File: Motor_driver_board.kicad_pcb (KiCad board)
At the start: 2 copper layers, 20 parts, among them J1 USB_B_Micro, U1 LM2596DSADJG, U10 NTMFS5C628NLT1G, U11 NTMFS5C628NLT1G, U12 NTMFS5C628NLT1G, U13 LM393, U2 TPS62A01ADRL, U3 ESP32-S3-MINI-1, U4 USBLC6-2SC6, U5 DRV8323RSRGZR, U6 NTMFS5C628NLT1G, U7 NTMFS5C628NLT1G, U8 NTMFS5C628NLT1G, U9 NTMFS5C628NLT1G

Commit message: Layed out PCB
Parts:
- added C1: 470 uF, Capacitor_SMD:CP_Elec_10x12.5, F.Cu at (171.5, 55.1)
- added C10: 22 uF, Capacitor_SMD:C_0603_1608Metric, F.Cu at (174.1, 130.7)
- added C11: 1 uF, Capacitor_SMD:C_0402_1005Metric, F.Cu at (149.4, 125.2)
- added C12: 0.1 uF, Capacitor_SMD:C_0402_1005Metric, F.Cu at (178.4, 91.9)
- added C13: 1 uF, Capacitor_SMD:C_0402_1005Metric, F.Cu at (178.2, 115.6)
- added C14: 47 nF, Capacitor_SMD:C_0603_1608Metric, F.Cu at (183.5, 105.2)
- added C15: 1 uF, Capacitor_SMD:C_0402_1005Metric, F.Cu at (182.5, 115.1)
- added C16: 1 uF, Capacitor_SMD:C_0402_1005Metric, F.Cu at (180.5, 105.9)
- added C17: 0.1 uF, Capacitor_SMD:C_0603_1608Metric, F.Cu at (180.5, 104.6)
- added C18: 2.2 uF, Capacitor_SMD:C_0805_2012Metric, F.Cu at (194.7, 102.6)
- added C19: 470 uF, Capacitor_SMD:CP_Elec_10x12.5, F.Cu at (183.0, 55.0)
- added C20: 470 uF, Capacitor_SMD:CP_Elec_10x12.5, F.Cu at (194.6, 55.1)
- added C21: 220 uF, Capacitor_SMD:CP_Elec_6.3x7.7, F.Cu at (164.8, 105.5)
- added C22: 2.2 uF, Capacitor_SMD:C_0805_2012Metric, F.Cu at (194.4, 90.2)
- added C23: 2.2 uF, Capacitor_SMD:C_0805_2012Metric, F.Cu at (194.2, 77.9)
- added C24: 0.1 uF, Capacitor_SMD:C_0402_1005Metric, F.Cu at (93.6, 85.7)
- added C25: 1 nF, Capacitor_SMD:C_0402_1005Metric, F.Cu at (175.8, 121.7)
- added C26: 1 nF, Capacitor_SMD:C_0402_1005Metric, F.Cu at (174.8, 123.2)
- added C27: 1 nF, Capacitor_SMD:C_0402_1005Metric, F.Cu at (172.8, 124.1)
- added C28: 100 uF, Capacitor_SMD:CP_Elec_8x10, F.Cu at (177.5, 69.5)
- added C3: 15 nF, Capacitor_SMD:C_0402_1005Metric, F.Cu at (181.3, 90.4)
- added C4: 4.7 uF, Capacitor_SMD:C_0603_1608Metric, F.Cu at (153.7, 108.5)
- added C5: 10 pF, Capacitor_SMD:C_0402_1005Metric, F.Cu at (153.2, 97.4)
- added C6: 22 uF, Capacitor_SMD:C_0603_1608Metric, F.Cu at (153.5, 96.0)
- added C7: 4.7 uF, Capacitor_SMD:C_0805_2012Metric, F.Cu at (177.4, 74.9)
- added C8: 0.1 uF, Capacitor_SMD:C_0402_1005Metric, F.Cu at (137.5, 90.8)
- added C9: 0.1 uF, Capacitor_SMD:C_0402_1005Metric, F.Cu at (172.8, 130.2)
- added FID1: Fiducial, Fiducial:Fiducial_1mm_Mask2mm, F.Cu at (58.8, 36.8)
- added FID2: Fiducial, Fiducial:Fiducial_1mm_Mask2mm, F.Cu at (58.8, 40.4)
- added FID3: Fiducial, Fiducial:Fiducial_1mm_Mask2mm, F.Cu at (58.8, 43.9)
- added H1: MountingHole, MountingHole:MountingHole_3.2mm_M3, F.Cu at (133.9, 53.1)
- added H2: MountingHole, MountingHole:MountingHole_3.2mm_M3, F.Cu at (133.9, 133.1)
- added H3: MountingHole, MountingHole:MountingHole_3.2mm_M3, F.Cu at (213.9, 133.1)
- added H4: MountingHole, MountingHole:MountingHole_3.2mm_M3, F.Cu at (213.9, 53.1)
- added J2: Screw_Terminal_01x02, TerminalBlocks:TerminalBlock_MetzConnect_Type703_RT10N02HGLU_1x02_P9.52mm_Horizontal, F.Cu at (213.5, 82.8)
- added J3: Screw_Terminal_01x02, TerminalBlocks:TerminalBlock_MetzConnect_Type703_RT10N02HGLU_1x02_P9.52mm_Horizontal, F.Cu at (214.0, 62.7)
- added J4: Screw_Terminal_01x03, TerminalBlocks:TerminalBlock_MetzConnect_Type703_RT10N03HGLU_1x03_P9.52mm_Horizontal, F.Cu at (213.4, 104.3)
- added L1: 33 uH, Inductor_SMD:L_TechFuse_SL0630, F.Cu at (163.1, 97.3)
- added L2: 1.0 uH, Inductor_SMD:L_1008_2520Metric, F.Cu at (153.3, 102.5)
- added NT1: NetTie_2, NetTie:NetTie-2_SMD_Pad0.5mm, F.Cu at (192.3, 91.9)
- added R1: 3.1k, Resistor_SMD:R_0603_1608Metric, F.Cu at (181.2, 89.1)
- added R10: 100 ohm, Resistor_SMD:R_0603_1608Metric, F.Cu at (177.9, 121.9)
- added R11: 10k, Resistor_SMD:R_0603_1608Metric, F.Cu at (178.2, 117.1)
- added R12: 150k, Resistor_SMD:R_0603_1608Metric, F.Cu at (159.9, 57.0)
- added R13: 10k, Resistor_SMD:R_0603_1608Metric, F.Cu at (159.9, 53.2)
- added R14: 10k, Resistor_SMD:R_0603_1608Metric, F.Cu at (163.4, 59.7)
- added R15: 10k, Resistor_SMD:R_0603_1608Metric, F.Cu at (162.7, 62.2)
- added R16: 10k, Resistor_SMD:R_0603_1608Metric, F.Cu at (163.3, 65.0)
- added R17: 1000k, Resistor_SMD:R_0603_1608Metric, F.Cu at (165.0, 65.0)
- added R18: 10 k, Resistor_SMD:R_0603_1608Metric, F.Cu at (169.5, 115.6)
- added R19: 100 ohm, Resistor_SMD:R_0603_1608Metric, F.Cu at (176.8, 123.4)
- added R2: 1.0k, Resistor_SMD:R_0603_1608Metric, F.Cu at (181.2, 91.7)
- added R20: 100 ohm, Resistor_SMD:R_0603_1608Metric, F.Cu at (174.9, 125.0)
- added R3: 470 k, Resistor_SMD:R_0603_1608Metric, F.Cu at (153.2, 98.8)
- added R4: 100k, Resistor_SMD:R_0603_1608Metric, F.Cu at (156.3, 101.7)
- added R5: 10 k, Resistor_SMD:R_0603_1608Metric, F.Cu at (148.8, 126.5)
- added R6: 10 k, Resistor_SMD:R_0603_1608Metric, F.Cu at (179.8, 128.0)
- added R7: 0.002 ohm, Resistor_SMD:R_2512_6332Metric, F.Cu at (192.4, 108.3)
- added R8: 0.002 ohm, Resistor_SMD:R_2512_6332Metric, F.Cu at (192.6, 95.9)
- added R9: 0.002 ohm, Resistor_SMD:R_2512_6332Metric, F.Cu at (192.7, 83.2)
- added SW1: Boot, SMD_Button:SW_3x6_SMD_LCSC, F.Cu at (183.8, 128.1)
- added SW2: Reset, SMD_Button:SW_3x6_SMD_LCSC, F.Cu at (152.9, 128.4)
- U1: footprint Package_TO_SOT_SMD:TO-263-5_TabPin3 -> Package_TO_SOT_SMD:TO-263-5_TabPin6
- moved J1 111.1 mm to (131.5, 91.2), turned to -90 degrees
- moved U7 98.5 mm to (199.6, 65.5), turned to 90 degrees
- moved U12 88.3 mm to (200.2, 77.7), turned to 180 degrees
- moved U6 87.4 mm to (199.9, 102.6), turned to 180 degrees
- moved U8 85.3 mm to (200.2, 83.9), turned to 0 degrees
- moved U10 84.5 mm to (200.2, 90.3), turned to 180 degrees
- moved U11 84.4 mm to (200.2, 96.5), turned to 0 degrees
- moved U9 84.0 mm to (199.9, 108.8)
- moved U3 74.8 mm to (164.3, 127.7), turned to 180 degrees
- moved D1 71.5 mm to (164.6, 111.2)
- moved U5 70.0 mm to (180.0, 110.6), turned to -90 degrees
- moved D3 55.4 mm to (184.6, 66.8), turned to -90 degrees
- moved U13 46.8 mm to (161.0, 70.4), turned to -90 degrees
- moved D4 45.5 mm to (170.3, 67.1), turned to 90 degrees
- moved U1 45.0 mm to (169.4, 82.0)
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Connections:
- J1 pad 2: Net-(J1-D-) -> /ESP32_S3_mini/D-
- J1 pad 3: Net-(J1-D+) -> /ESP32_S3_mini/D+
- U12 pad 1: Net-(U5-SHC) -> /DRV8323/PhaseC
- U12 pad 2: Net-(U5-SHC) -> /DRV8323/PhaseC
- U12 pad 3: Net-(U5-SHC) -> /DRV8323/PhaseC
- U2 pad 6: /Power_distro/PG -> /ESP32_S3_mini/PG
- U3 pad 10: SOCA -> Net-(U3-IO6)
- U3 pad 11: SOCB -> Net-(U3-IO7)
- U3 pad 12: SOCC -> Net-(U3-IO8)
- U3 pad 18: unconnected-(U3-IO14-Pad18) -> FAULT
- U3 pad 23: Net-(U3-USB_D-) -> /ESP32_S3_mini/D-
- U3 pad 24: Net-(U3-USB_D+) -> /ESP32_S3_mini/D+
- U3 pad 5: unconnected-(U3-IO1-Pad5) -> DRVEn
- U4 pad 1: Net-(J1-D+) -> /ESP32_S3_mini/D+
- U4 pad 3: Net-(J1-D-) -> /ESP32_S3_mini/D-
- U4 pad 4: Net-(U3-USB_D-) -> /ESP32_S3_mini/D-
- U4 pad 6: Net-(U3-USB_D+) -> /ESP32_S3_mini/D+
- U5 pad 19: Net-(U5-SHC) -> /DRV8323/PhaseC
- U5 pad 28: /DRV8323/MCU -> FAULT
- U5 pad 33: /DRV8323/MCU -> DRVEn
- U7 pad 5: +24V -> Net-(J3-Pin_1)
- U7 pad 6: +24V -> Net-(J3-Pin_1)
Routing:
- net Net-(D5-A): track 0.00 -> 15.7 mm, vias 0 -> 2
- net /ESP32_S3_mini/D-: track 0.00 -> 7.87 mm
- net /ESP32_S3_mini/D+: track 0.00 -> 7.83 mm
- net GND: track 0.00 -> 1.04 mm, vias 0 -> 1
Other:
- board outline added: 90 x 90 mm
- copper layers 2 -> 4

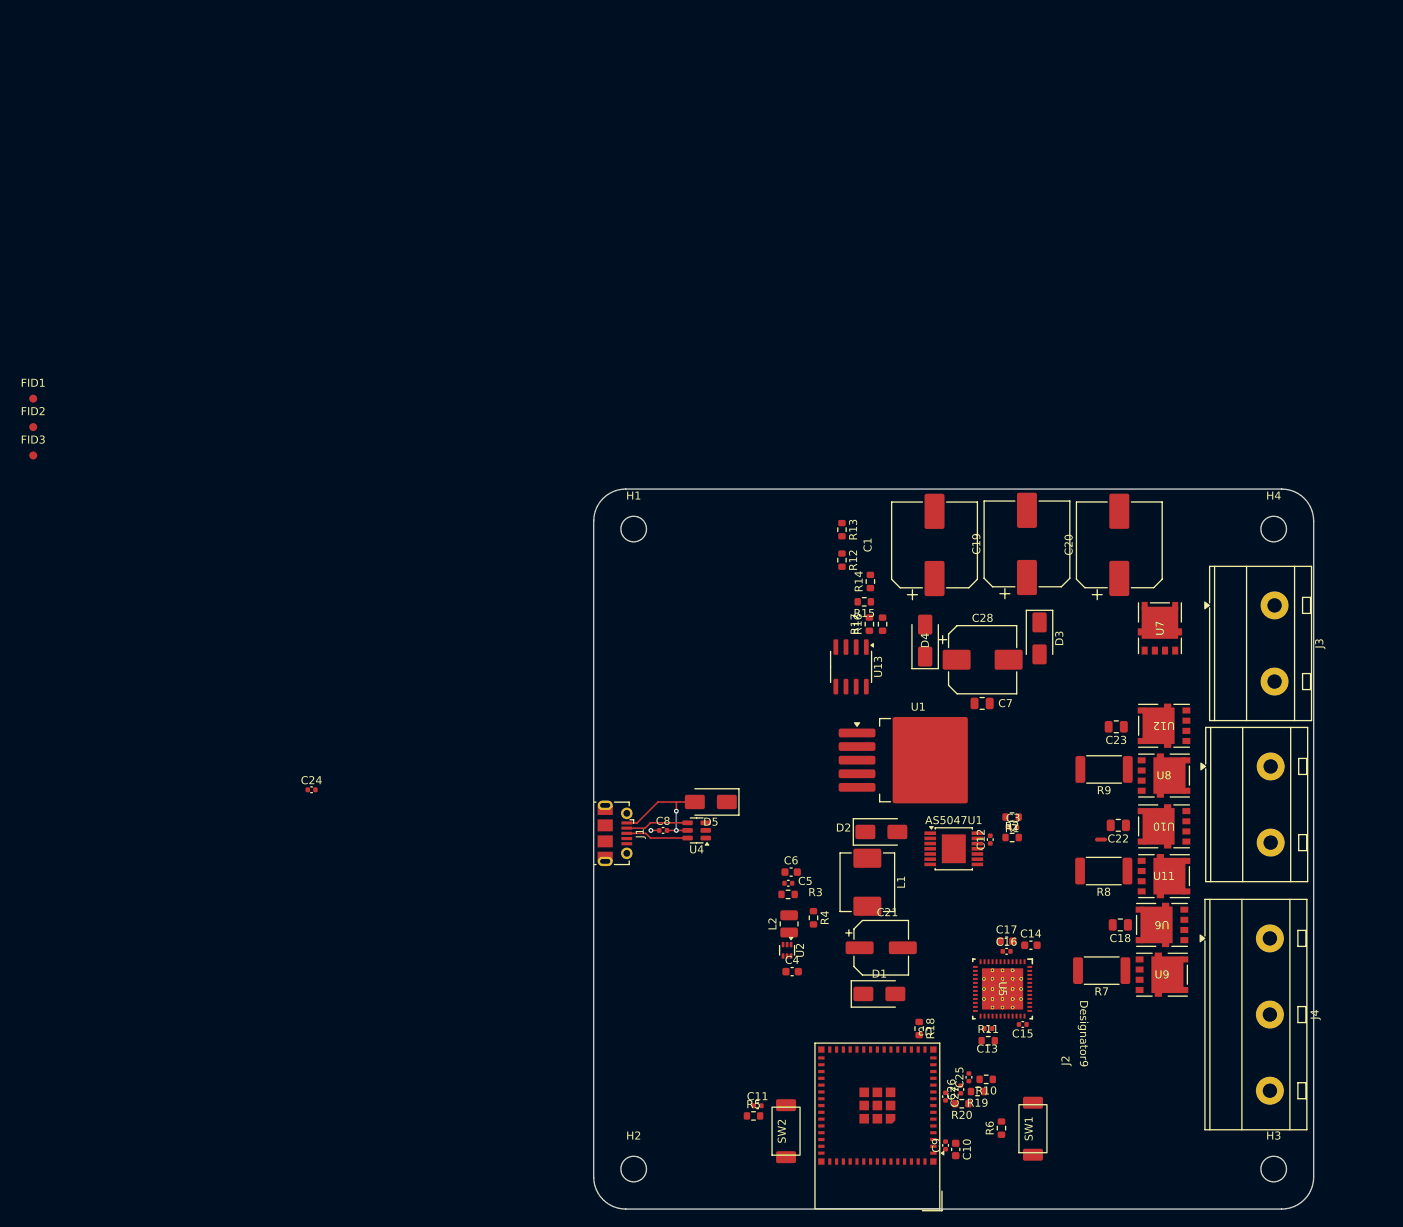
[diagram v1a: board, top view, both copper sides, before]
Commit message: finalizing PCB Layouts and traces
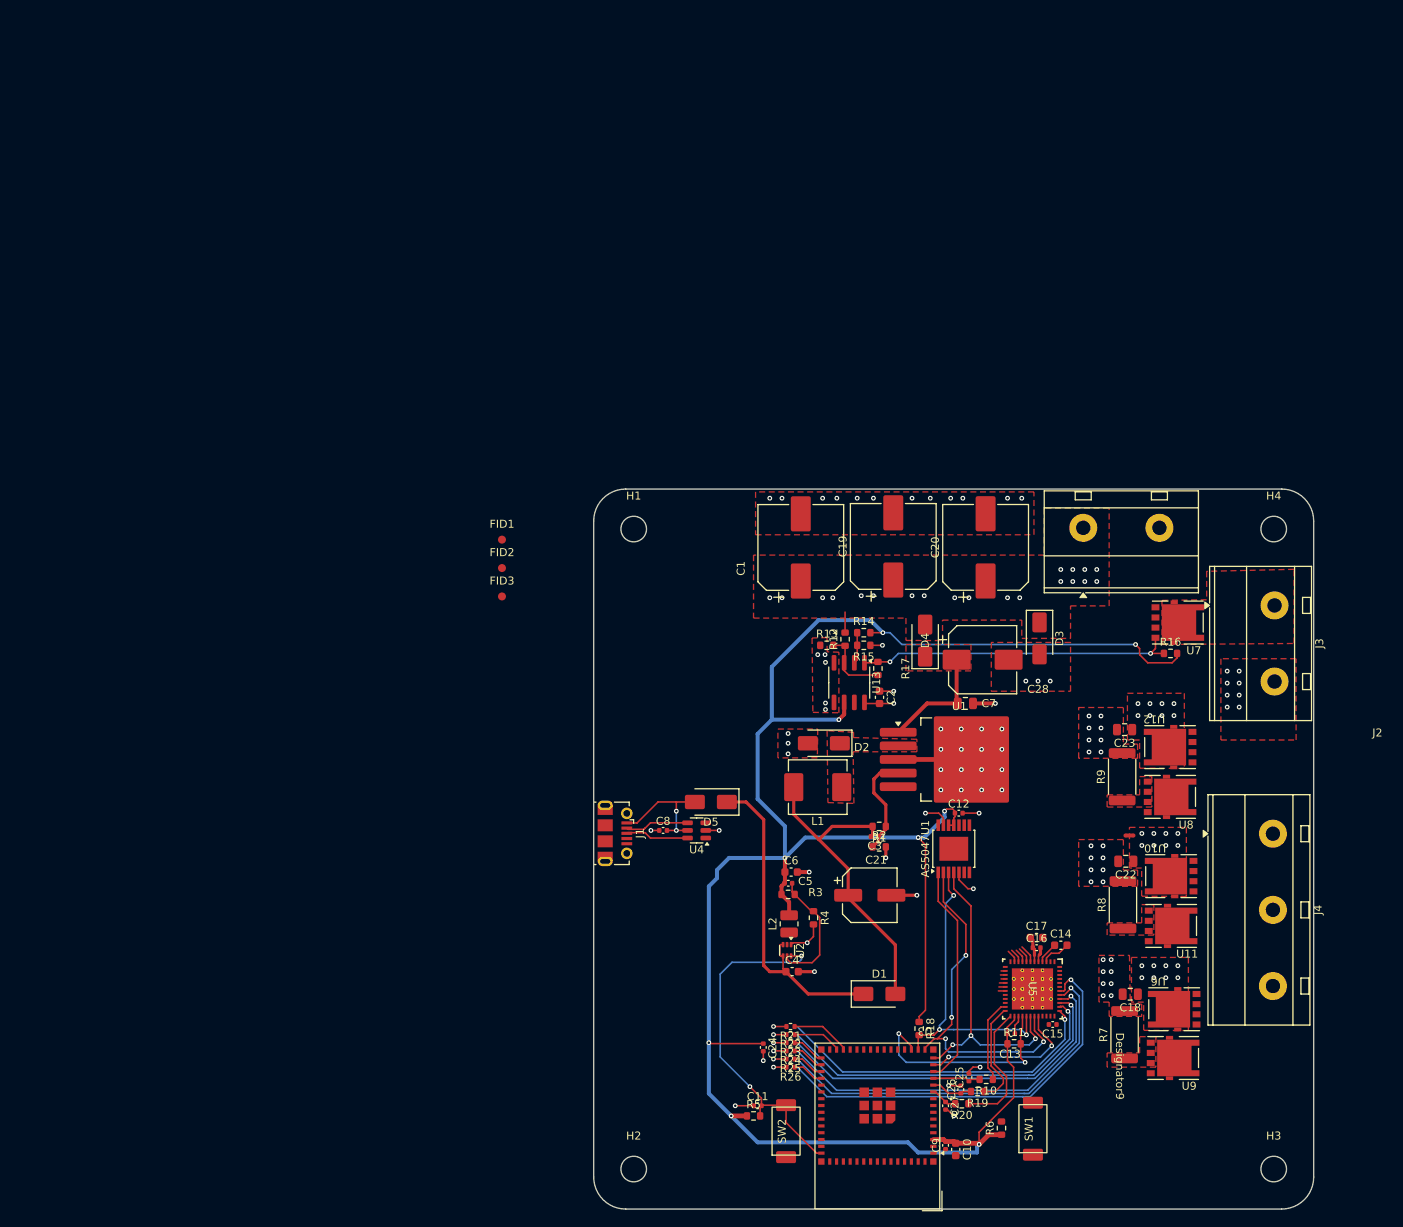
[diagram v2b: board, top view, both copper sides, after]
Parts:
- added C2: 0.1 uF, Capacitor_SMD:C_0603_1608Metric, F.Cu at (164.6, 74.2)
- added R21: 33 ohm, Resistor_SMD:R_0402_1005Metric, F.Cu at (153.5, 115.3)
- added R22: 33 ohm, Resistor_SMD:R_0402_1005Metric, F.Cu at (153.5, 116.3)
- added R23: 33 ohm, Resistor_SMD:R_0402_1005Metric, F.Cu at (153.5, 117.3)
- added R24: 33 ohm, Resistor_SMD:R_0402_1005Metric, F.Cu at (153.5, 118.4)
- added R25: 33 ohm, Resistor_SMD:R_0402_1005Metric, F.Cu at (153.5, 119.4)
- added R26: 33 ohm, Resistor_SMD:R_0402_1005Metric, F.Cu at (153.5, 120.4)
- U10, U11, U12, U6, U7, U8, U9: footprint ESP-32-S3-MINI-1:DFN5_5X6_ONS -> ESP-32-S3-MINI-1:NTMF_FET_FIXED
- moved C24 65.0 mm to (150.1, 117.9), turned to -90 degrees
- moved FID1 61.2 mm to (117.4, 54.5)
- moved FID2 61.2 mm to (117.4, 58.0)
- moved FID3 61.2 mm to (117.4, 61.6)
- moved J2 37.9 mm to (190.1, 53.0), turned to 0 degrees
- moved R16 37.8 mm to (201.0, 68.7), turned to 0 degrees
- moved C3 17.3 mm to (164.0, 91.6), turned to 180 degrees
- moved C1 16.7 mm to (154.8, 55.4)
- moved C19 16.7 mm to (166.3, 55.3)
- moved C20 16.7 mm to (177.9, 55.4)
- moved R1 16.7 mm to (164.6, 90.3)
- moved R2 16.7 mm to (164.6, 92.9)
- moved R13 14.6 mm to (158.0, 67.7), turned to 0 degrees
- moved L1 13.4 mm to (156.9, 85.4), turned to 180 degrees
- moved D2 13.2 mm to (157.6, 79.9), turned to 180 degrees
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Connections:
- R10 pad 2: Net-(U3-IO6) -> Net-(U3-IO8)
- R20 pad 2: Net-(U3-IO8) -> Net-(U3-IO6)
- U3 pad 28: INHA -> Net-(U3-IO33)
- U3 pad 29: INLA -> Net-(U3-IO34)
- U3 pad 31: INHB -> Net-(U3-IO35)
- U3 pad 32: INLB -> Net-(U3-IO36)
- U3 pad 33: INHC -> Net-(U3-IO37)
- U3 pad 34: INLC -> Net-(U3-IO38)
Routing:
- net +3.3V: track 0.00 -> 265.0 mm, vias 0 -> 9
- net INLC: track 0.00 -> 52.6 mm, vias 0 -> 2
- net INHC: track 0.00 -> 50.4 mm, vias 0 -> 2
- net GND: track 1.04 -> 50.5 mm, vias 1 -> 81
- net INLB: track 0.00 -> 48.6 mm, vias 0 -> 2
- net INHB: track 0.00 -> 45.9 mm, vias 0 -> 2
- net INLA: track 0.00 -> 44.7 mm, vias 0 -> 2
- net SLCK: track 0.00 -> 44.6 mm, vias 0 -> 4
- net /ESP32_S3_mini/PG: track 0.00 -> 43.9 mm, vias 0 -> 2
- net INHA: track 0.00 -> 42.9 mm, vias 0 -> 2
- net +5V: track 0.00 -> 41.9 mm
- net Net-(U7-GATE): track 0.00 -> 40.1 mm, vias 0 -> 2
- net Net-(D1-A): track 0.00 -> 39.9 mm
- net MOSI: track 0.00 -> 39.1 mm, vias 0 -> 3
- net MISO: track 0.00 -> 38.8 mm, vias 0 -> 3
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- added copper zone on F.Cu, net +24V
- added copper zone on F.Cu, net /DRV8323/CurrentSense_A
- added copper zone on F.Cu, net /DRV8323/CurrentSense_B
- added copper zone on F.Cu, net /DRV8323/CurrentSense_C
- added copper zone on F.Cu, net GND
- added copper zone on F.Cu, net Net-(D2-K)
- added copper zone on F.Cu, net Net-(D4-K)
- added copper zone on F.Cu, net Net-(J3-Pin_1)

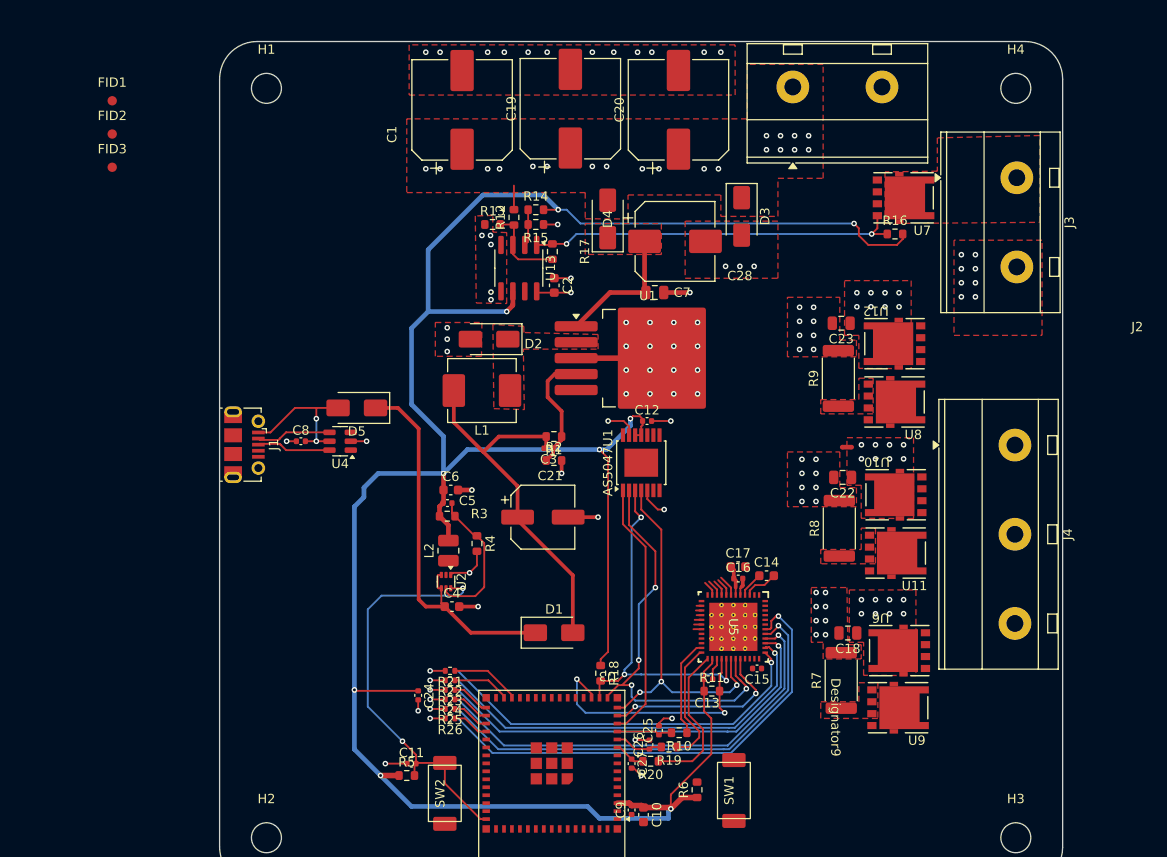
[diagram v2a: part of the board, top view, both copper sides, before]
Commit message: removed unnecessary regulators and replaced with cheaper buck
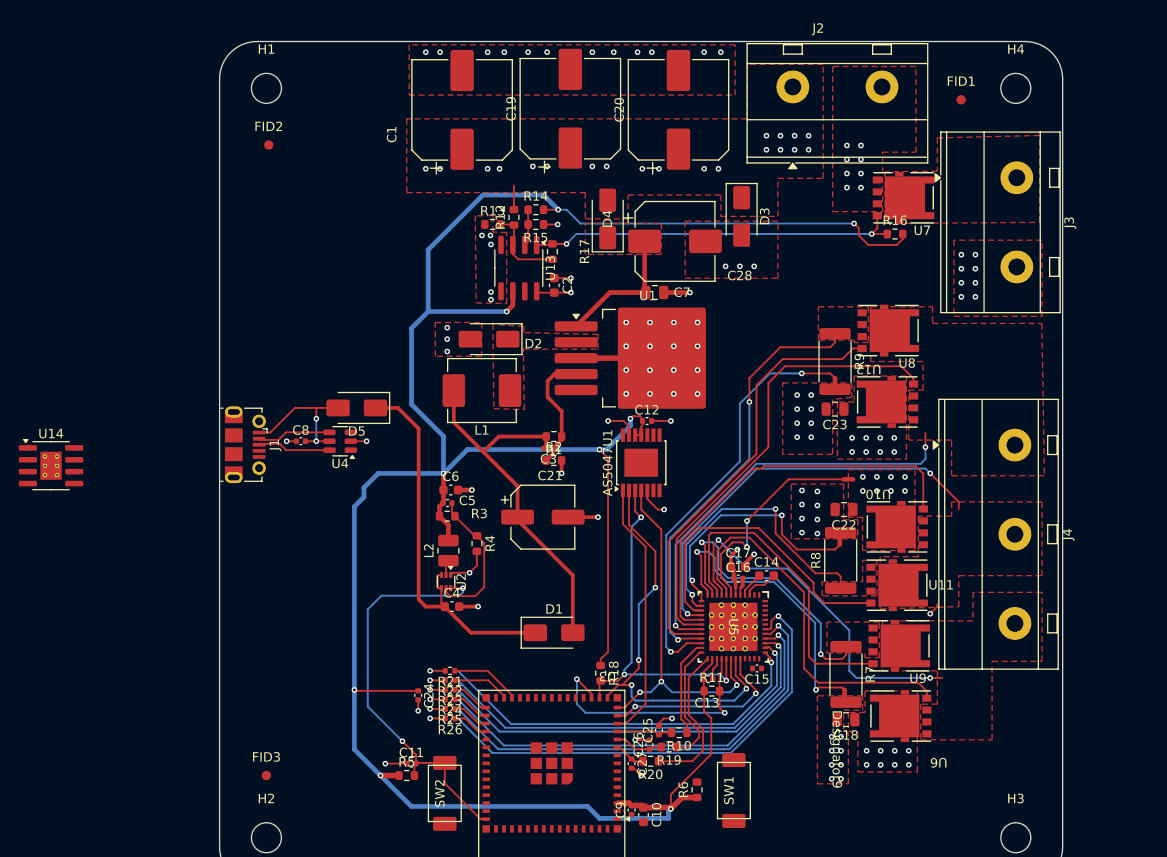
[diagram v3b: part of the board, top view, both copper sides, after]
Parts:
- added NT2: NetTie_2, NetTie:NetTie-2_SMD_Pad0.5mm, F.Cu at (194.6, 84.6)
- added NT3: NetTie_2, NetTie:NetTie-2_SMD_Pad0.5mm, F.Cu at (195.1, 101.3)
- added NT4: NetTie_2, NetTie:NetTie-2_SMD_Pad0.5mm, F.Cu at (195.6, 117.9)
- added U14: ~, ESP-32-S3-MINI-1:AP64200SP-13, F.Cu at (110.9, 93.4)
- moved FID1 90.6 mm to (208.0, 54.4)
- moved FID3 67.0 mm to (133.9, 126.5)
- moved FID2 16.8 mm to (134.1, 59.2)
- moved C18 9.25 mm to (195.7, 120.5)
- moved C23 9.19 mm to (194.6, 87.4)
- moved U8 7.65 mm to (200.3, 79.0)
- moved U6 6.99 mm to (201.6, 120.1)
- moved U9 6.61 mm to (201.4, 112.6)
- moved U12 6.27 mm to (200.2, 86.6)
- moved R8 3.43 mm to (195.2, 103.5)
- moved U10 3.43 mm to (201.2, 99.9)
- moved U11 3.43 mm to (201.2, 106.2)
- moved C22 3.43 mm to (195.5, 98.1)
- moved NT1 3.43 mm to (196.0, 94.9)
- moved R9 1.84 mm to (194.6, 82.3), turned to -90 degrees
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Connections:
- U5 pad 12: GND -> /DRV8323/CurrA
- U5 pad 13: GND -> /DRV8323/CurrB
- U5 pad 22: GND -> /DRV8323/CurrC
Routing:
- net Net-(U12-GATE): track 0.80 -> 49.4 mm
- net Net-(U5-GLC): track 0.00 -> 46.5 mm
- net /DRV8323/CurrentSense_C: track 0.00 -> 46.0 mm, vias 0 -> 2
- net /DRV8323/CurrC: track 0.00 -> 45.3 mm, vias 0 -> 2
- net /DRV8323/PhaseB: track 0.53 -> 45.7 mm, vias 0 -> 3
- net /DRV8323/PhaseC: track 0.86 -> 44.8 mm, vias 0 -> 2
- net Net-(U10-GATE): track 0.73 -> 43.8 mm
- net Net-(U5-GHA): track 1.96 -> 40.4 mm
- net /DRV8323/PhaseA: track 1.76 -> 39.0 mm, vias 0 -> 2
- net Net-(U11-GATE): track 0.59 -> 33.4 mm
- net Net-(U5-GLA): track 1.78 -> 34.5 mm
- net /DRV8323/CurrA: track 0.00 -> 32.0 mm, vias 0 -> 2
- net /DRV8323/CurrentSense_B: track 0.53 -> 31.3 mm, vias 0 -> 2
- net /DRV8323/CurrentSense_A: track 1.62 -> 30.9 mm, vias 0 -> 2
- net /DRV8323/CurrB: track 0.00 -> 26.7 mm, vias 0 -> 2
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- added copper zone on In2.Cu, net +24V
- added copper zone on F.Cu, net /DRV8323/PhaseA
- added copper zone on F.Cu, net /DRV8323/PhaseB
- added copper zone on F.Cu, net /DRV8323/PhaseC
- added copper zone on In1.Cu, net GND
